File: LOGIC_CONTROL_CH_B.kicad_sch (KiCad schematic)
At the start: 47 parts, among them IC60 ${DEVICE}, IC61 ${DEVICE}, IC62 ${DEVICE}, IC63 ${DEVICE}, IC64 ${DEVICE}, IC65 ${DEVICE}, IC66 ${DEVICE}

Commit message: Updated schematic and rerouted PCB
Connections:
- net VCCA renamed VCCB
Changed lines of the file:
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@@
 		)
 	)
-	(label "VCCA"
+	(label "VCCB"
 		(at 300.99 212.09 0)
 		(effects
@@
 		)
 	)
-	(label "VCCA"
+	(label "VCCB"
 		(at 308.61 184.15 180)
 		(effects

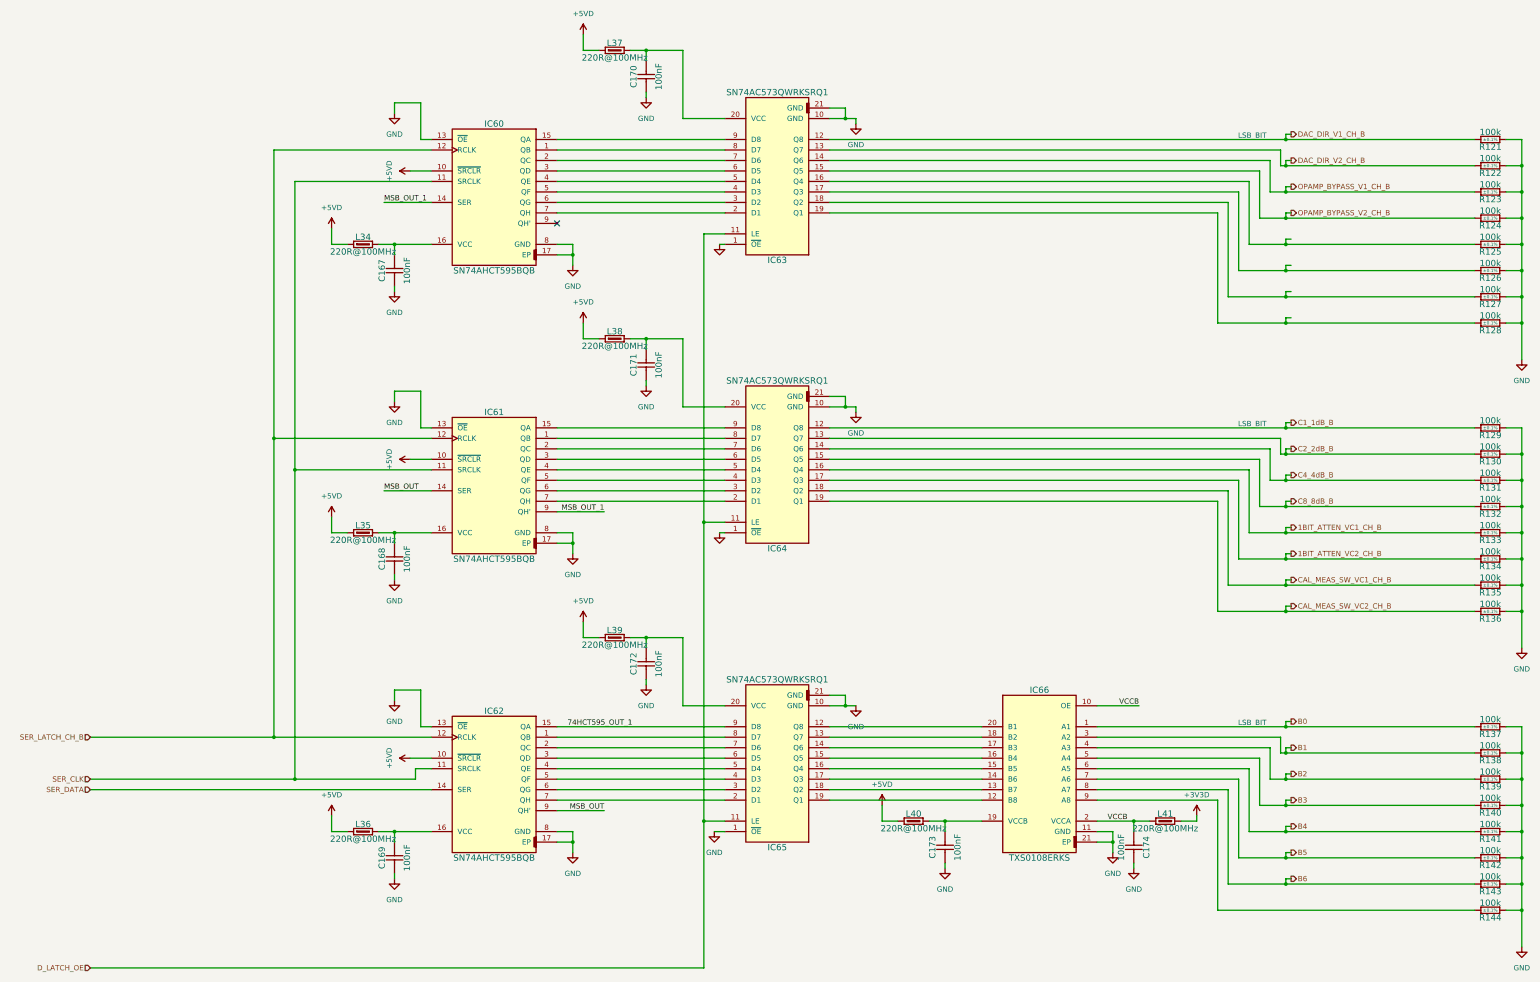
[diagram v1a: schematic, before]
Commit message: Rerouted PCB Logic part
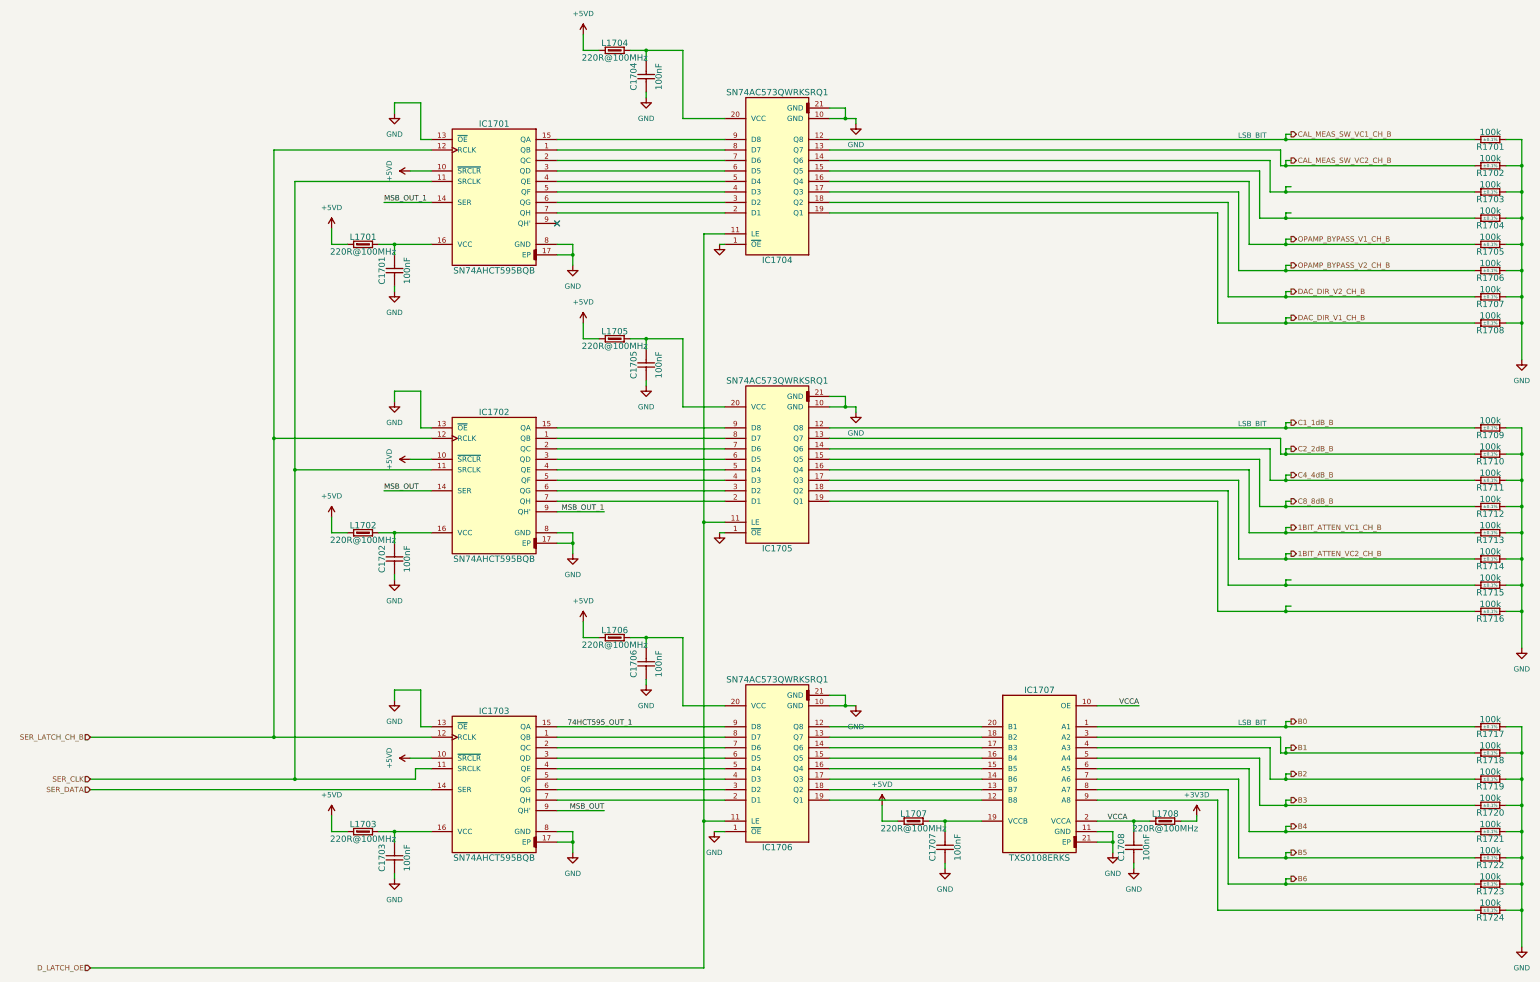
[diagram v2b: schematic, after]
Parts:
- renumbered C167 to C1701, C168 to C1702, C169 to C1703, C170 to C1704, C171 to C1705, C172 to C1706, C173 to C1707, C174 to C1708, IC60 to IC1701, IC61 to IC1702, IC62 to IC1703, IC63 to IC1704, IC64 to IC1705, IC65 to IC1706, IC66 to IC1707, L34 to L1701, L35 to L1702, L36 to L1703, L37 to L1704, L38 to L1705, L39 to L1706, L40 to L1707, L41 to L1708, R121 to R1701, R122 to R1702, R123 to R1703, R124 to R1704, R125 to R1705, R126 to R1706, R127 to R1707, R128 to R1708, R129 to R1709, R130 to R1710, R131 to R1711, R132 to R1712, R133 to R1713, R134 to R1714, R135 to R1715, R136 to R1716, R137 to R1717, R138 to R1718, R139 to R1719, R140 to R1720, R141 to R1721, R142 to R1722, R143 to R1723, R144 to R1724
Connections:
- net CAL_MEAS_SW_VC1_CH_B: now also IC1704.12 (Q8), R1701.2; no longer IC1705.18 (Q2), R1715.2
- net CAL_MEAS_SW_VC2_CH_B: now also IC1704.13 (Q7), R1702.2; no longer IC1705.19 (Q1), R1716.2
- net DAC_DIR_V1_CH_B: now also IC1704.19 (Q1), R1708.2; no longer IC1704.12 (Q8), R1701.2
- net DAC_DIR_V2_CH_B: now also IC1704.18 (Q2), R1707.2; no longer IC1704.13 (Q7), R1702.2
- net GND: now also C1708.2; no longer C1708.1
- net OPAMP_BYPASS_V1_CH_B: now also IC1704.16 (Q4), R1705.2; no longer IC1704.14 (Q6), R1703.2
- net OPAMP_BYPASS_V2_CH_B: now also IC1704.17 (Q3), R1706.2; no longer IC1704.15 (Q5), R1704.2
- net VCCB renamed VCCA
- net VCCA: now also C1708.1; no longer C1708.2
- new net: IC1705.18 (Q2), R1715.2
- new net: IC1705.19 (Q1), R1716.2
- new net: IC1704.14 (Q6), R1703.2
- new net: IC1704.15 (Q5), R1704.2
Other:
- moved on the sheet: C1708

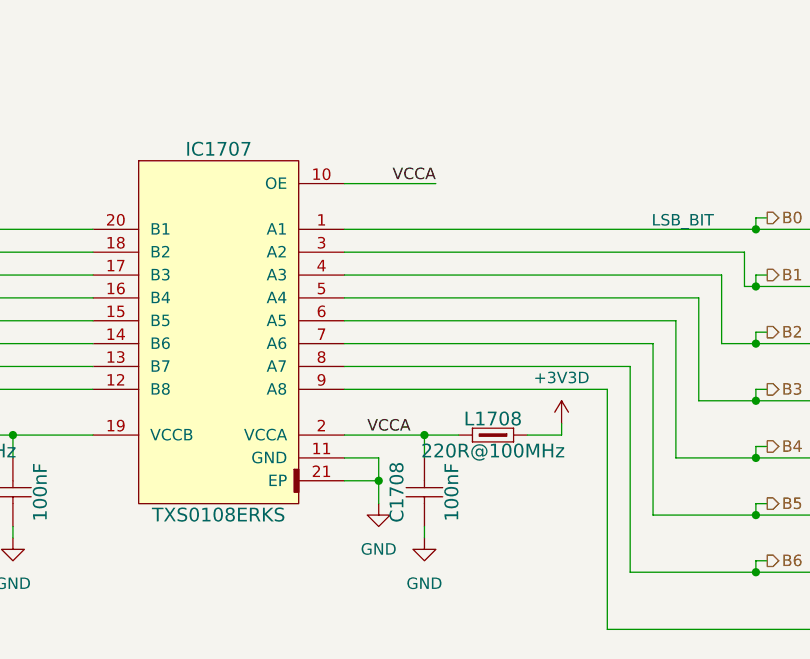
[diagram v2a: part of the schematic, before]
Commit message: Problems with nets
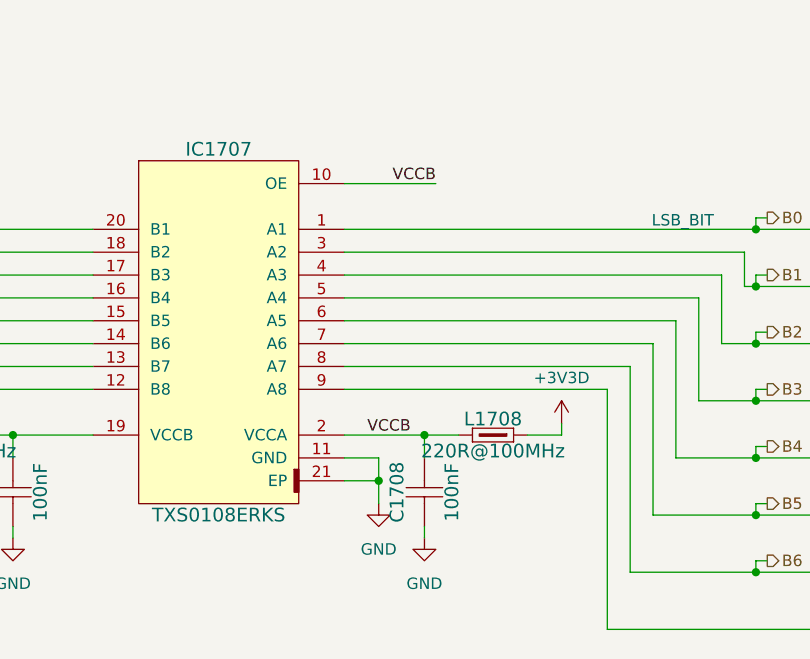
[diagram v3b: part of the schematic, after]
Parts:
- removed C1701, C1702, C1703, C1704, C1705, C1706, C1707, C1708: 100nF, Capacitors SMD:CAPC1005X55N, symbol CERN:Capacitors SMD/CC0402_100NF_25V_10%_X7R_YUDEN_TMK105B7104KVHF
- added C1701, C1702, C1703, C1704, C1705, C1706, C1707, C1708: 100nF, Capacitors SMD:CAPC1608X87N, symbol CERN:Capacitors SMD/CC0603_100NF_50V_10%_X7R
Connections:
- net GND: now also C1701.1, C1702.1, C1703.1, C1704.1, C1705.1, C1706.1, C1707.1, C1708.1
- net at IC1701.16 (VCC), L1701.1: now also C1701.2
- net at IC1704.20 (VCC), L1704.1: now also C1704.2
- net at IC1703.16 (VCC), L1703.1: now also C1703.2
- net at IC1705.20 (VCC), L1705.1: now also C1705.2
- net at IC1707.19 (VCCB), L1707.1: now also C1707.2
- net at IC1702.16 (VCC), L1702.1: now also C1702.2
- net at IC1706.20 (VCC), L1706.1: now also C1706.2
- net VCCA renamed VCCB
- net VCCB: now also C1708.2
